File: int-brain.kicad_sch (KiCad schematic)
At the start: 34 parts, among them J1 PWR, J10 Conn_01x19_Pin, J11 Conn_01x19_Pin, J2 UART0, J3 I2C0, J4 PWR, J5 1MA, J6 1MB, J7 2MA, J8 2MB, J9 MPU9250, U2 ESP32-DevKitC, U4 LM2576HVT-5

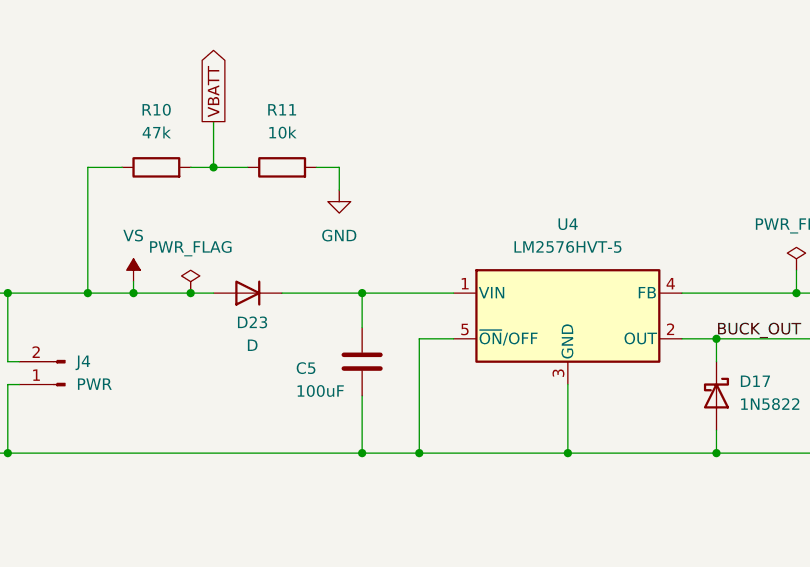
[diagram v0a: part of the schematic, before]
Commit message: placed PCB components
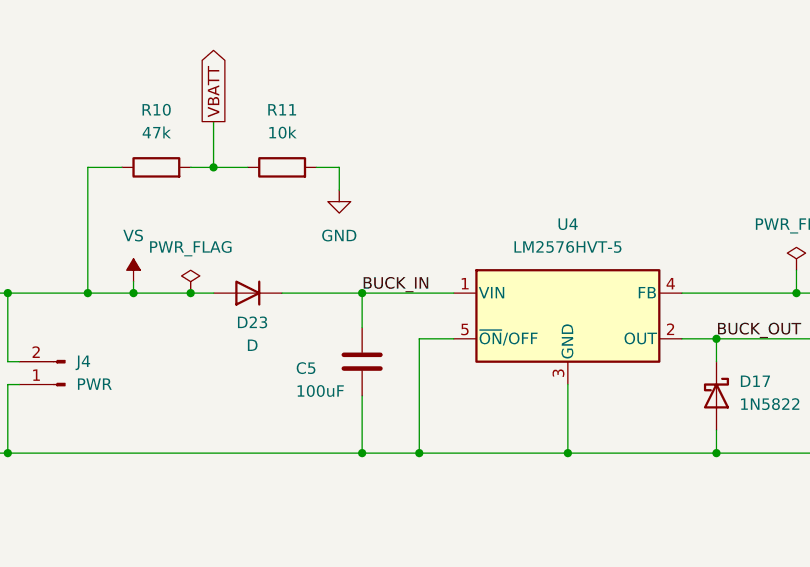
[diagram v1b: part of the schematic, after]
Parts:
- D18, D19, D20, D21, D22: footprint LED_THT:LED_D3.0mm -> LED_SMD:LED_0603_1608Metric_Pad1.05x0.95mm_HandSolder
- D23: footprint Diode_THT:D_DO-41_SOD81_P10.16mm_Horizontal -> Diode_SMD:D_SMA_Handsoldering
- R10, R11, R5, R6, R7, R8, R9: footprint Resistor_THT:R_Axial_DIN0207_L6.3mm_D2.5mm_P10.16mm_Horizontal -> Resistor_SMD:R_1206_3216Metric_Pad1.30x1.75mm_HandSolder
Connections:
- net BUCK_IN: now reaches C5.1, D23.1 (K), U4.1 (VIN)
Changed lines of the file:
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@@
 		)
 	)
+	(label "BUCK_IN"
+		(at 123.19 311.15 0)
+		(fields_autoplaced yes)
+		(effects
+			(font
+				(size 1.27 1.27)
+			)
+			(justify left bottom)
+		)
+	)
 	(label "1MB2"
 		(at 118.11 375.92 0)
@@
 			)
 		)
-		(property "Footprint" "LED_THT:LED_D3.0mm"
+		(property "Footprint" "LED_SMD:LED_0603_1608Metric_Pad1.05x0.95mm_HandSolder"
 			(at 257.81 146.05 0)
 			(effects
@@
 			)
 		)
-		(property "Footprint" "Resistor_THT:R_Axial_DIN0207_L6.3mm_D2.5mm_P10.16mm_Horizontal"
+		(property "Footprint" "Resistor_SMD:R_1206_3216Metric_Pad1.30x1.75mm_HandSolder"
 			(at 194.31 312.928 90)
 			(effects
@@
 			)
 		)
-		(property "Footprint" "Diode_THT:D_DO-41_SOD81_P10.16mm_Horizontal"
+		(property "Footprint" "Diode_SMD:D_SMA_Handsoldering"
 			(at 110.49 311.15 0)
 			(effects
@@
 			)
 		)
-		(property "Footprint" "Resistor_THT:R_Axial_DIN0207_L6.3mm_D2.5mm_P10.16mm_Horizontal"
+		(property "Footprint" "Resistor_SMD:R_1206_3216Metric_Pad1.30x1.75mm_HandSolder"
 			(at 238.252 134.62 90)
 			(effects
@@
 			)
 		)
-		(property "Footprint" "LED_THT:LED_D3.0mm"
+		(property "Footprint" "LED_SMD:LED_0603_1608Metric_Pad1.05x0.95mm_HandSolder"
 			(at 266.7 146.05 0)
 			(effects
@@
 			)
 		)
-		(property "Footprint" "LED_THT:LED_D3.0mm"
+		(property "Footprint" "LED_SMD:LED_0603_1608Metric_Pad1.05x0.95mm_HandSolder"
 			(at 248.92 146.05 0)
 			(effects
@@
 			)
 		)
-		(property "Footprint" "Resistor_THT:R_Axial_DIN0207_L6.3mm_D2.5mm_P10.16mm_Horizontal"
+		(property "Footprint" "Resistor_SMD:R_1206_3216Metric_Pad1.30x1.75mm_HandSolder"
 			(at 114.3 298.958 90)
 			(effects
@@
 			)
 		)
-		(property "Footprint" "Resistor_THT:R_Axial_DIN0207_L6.3mm_D2.5mm_P10.16mm_Horizontal"
+		(property "Footprint" "Resistor_SMD:R_1206_3216Metric_Pad1.30x1.75mm_HandSolder"
 			(at 256.032 134.62 90)
 			(effects
@@
 			)
 		)
-		(property "Footprint" "Resistor_THT:R_Axial_DIN0207_L6.3mm_D2.5mm_P10.16mm_Horizontal"
+		(property "Footprint" "Resistor_SMD:R_1206_3216Metric_Pad1.30x1.75mm_HandSolder"
 			(at 100.33 298.958 90)
 			(effects
@@
 			)
 		)
-		(property "Footprint" "Resistor_THT:R_Axial_DIN0207_L6.3mm_D2.5mm_P10.16mm_Horizontal"
+		(property "Footprint" "Resistor_SMD:R_1206_3216Metric_Pad1.30x1.75mm_HandSolder"
 			(at 264.922 134.62 90)
 			(effects
@@
 			)
 		)
-		(property "Footprint" "LED_THT:LED_D3.0mm"
+		(property "Footprint" "LED_SMD:LED_0603_1608Metric_Pad1.05x0.95mm_HandSolder"
 			(at 240.03 146.05 0)
 			(effects
@@
 			)
 		)
-		(property "Footprint" "LED_THT:LED_D3.0mm"
+		(property "Footprint" "LED_SMD:LED_0603_1608Metric_Pad1.05x0.95mm_HandSolder"
 			(at 200.66 321.31 0)
 			(effects
@@
 			)
 		)
-		(property "Footprint" "Resistor_THT:R_Axial_DIN0207_L6.3mm_D2.5mm_P10.16mm_Horizontal"
+		(property "Footprint" "Resistor_SMD:R_1206_3216Metric_Pad1.30x1.75mm_HandSolder"
 			(at 247.142 134.62 90)
 			(effects

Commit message: routing attempt
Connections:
- net BUCK_IN renamed VIN_BUCK
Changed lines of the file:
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@@
 		)
 	)
-	(label "BUCK_IN"
+	(label "VIN_BUCK"
 		(at 123.19 311.15 0)
 		(fields_autoplaced yes)

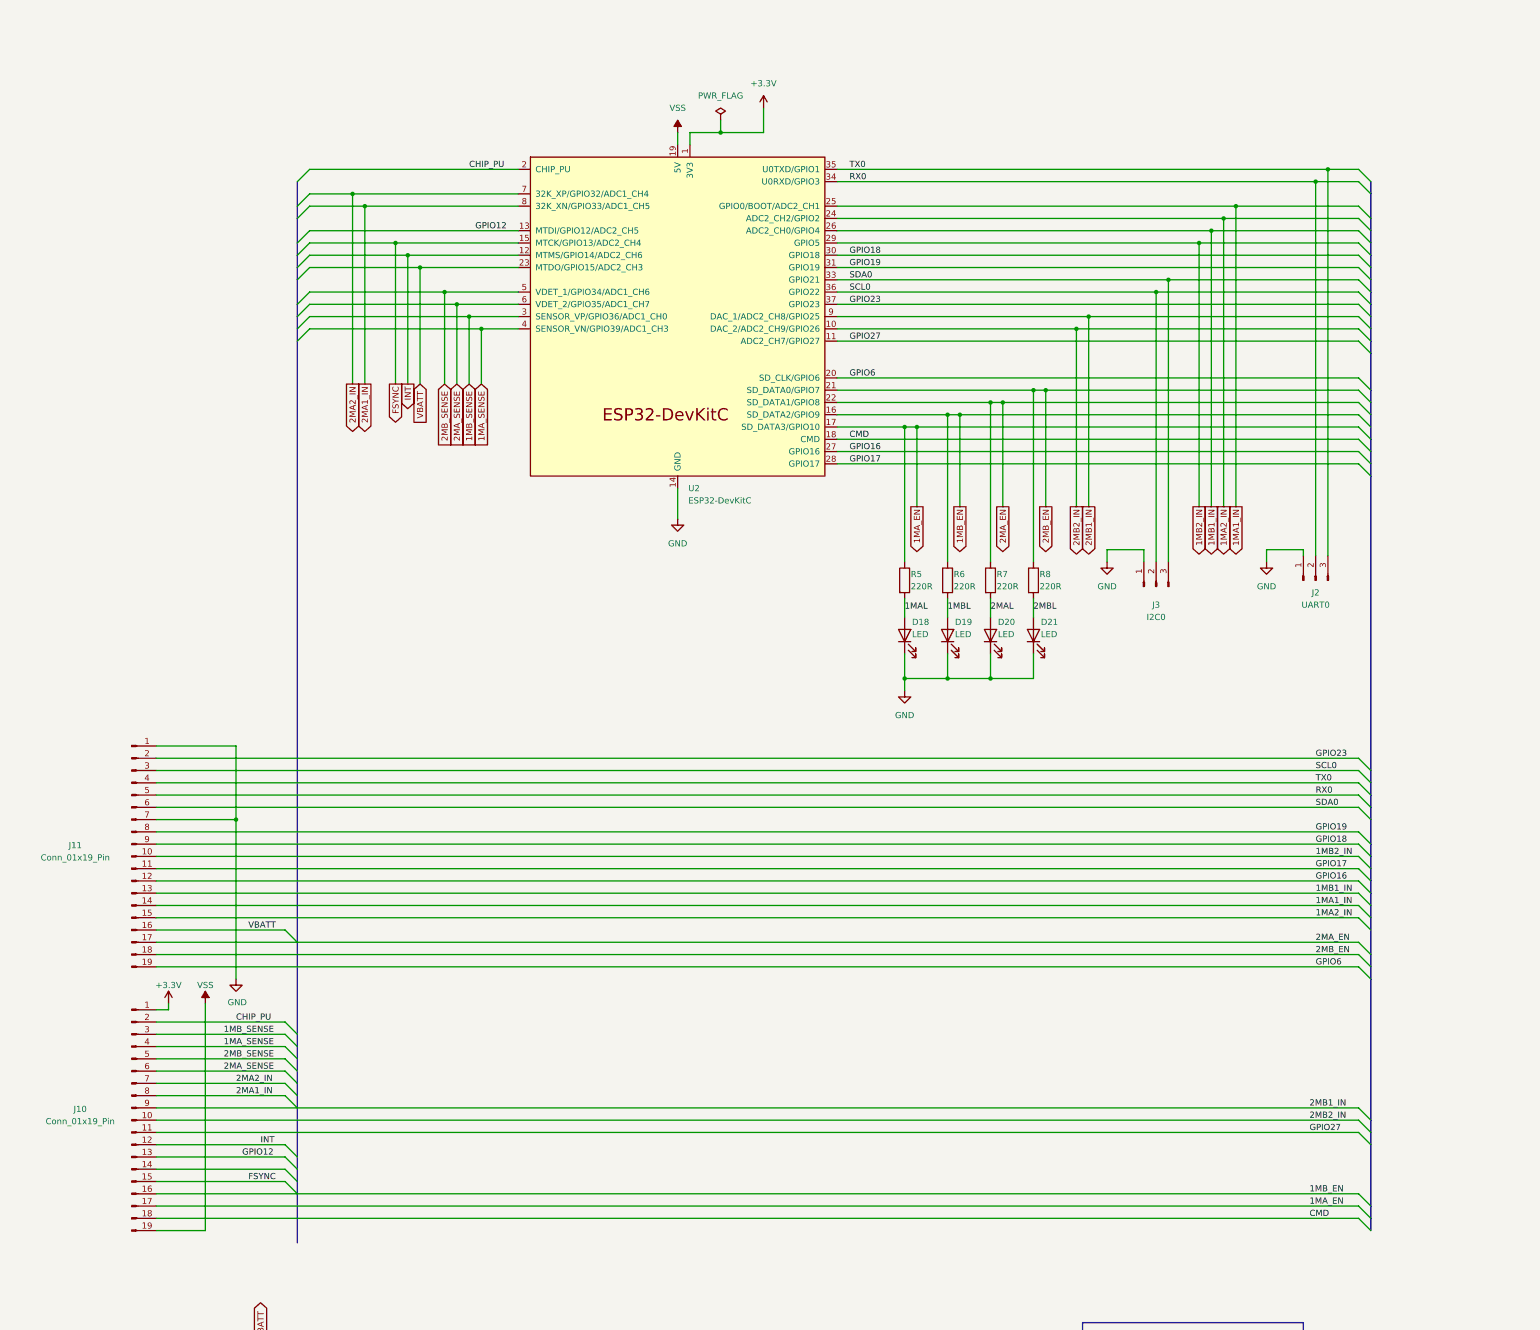
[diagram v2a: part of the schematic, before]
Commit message: re-do pinouts based on code
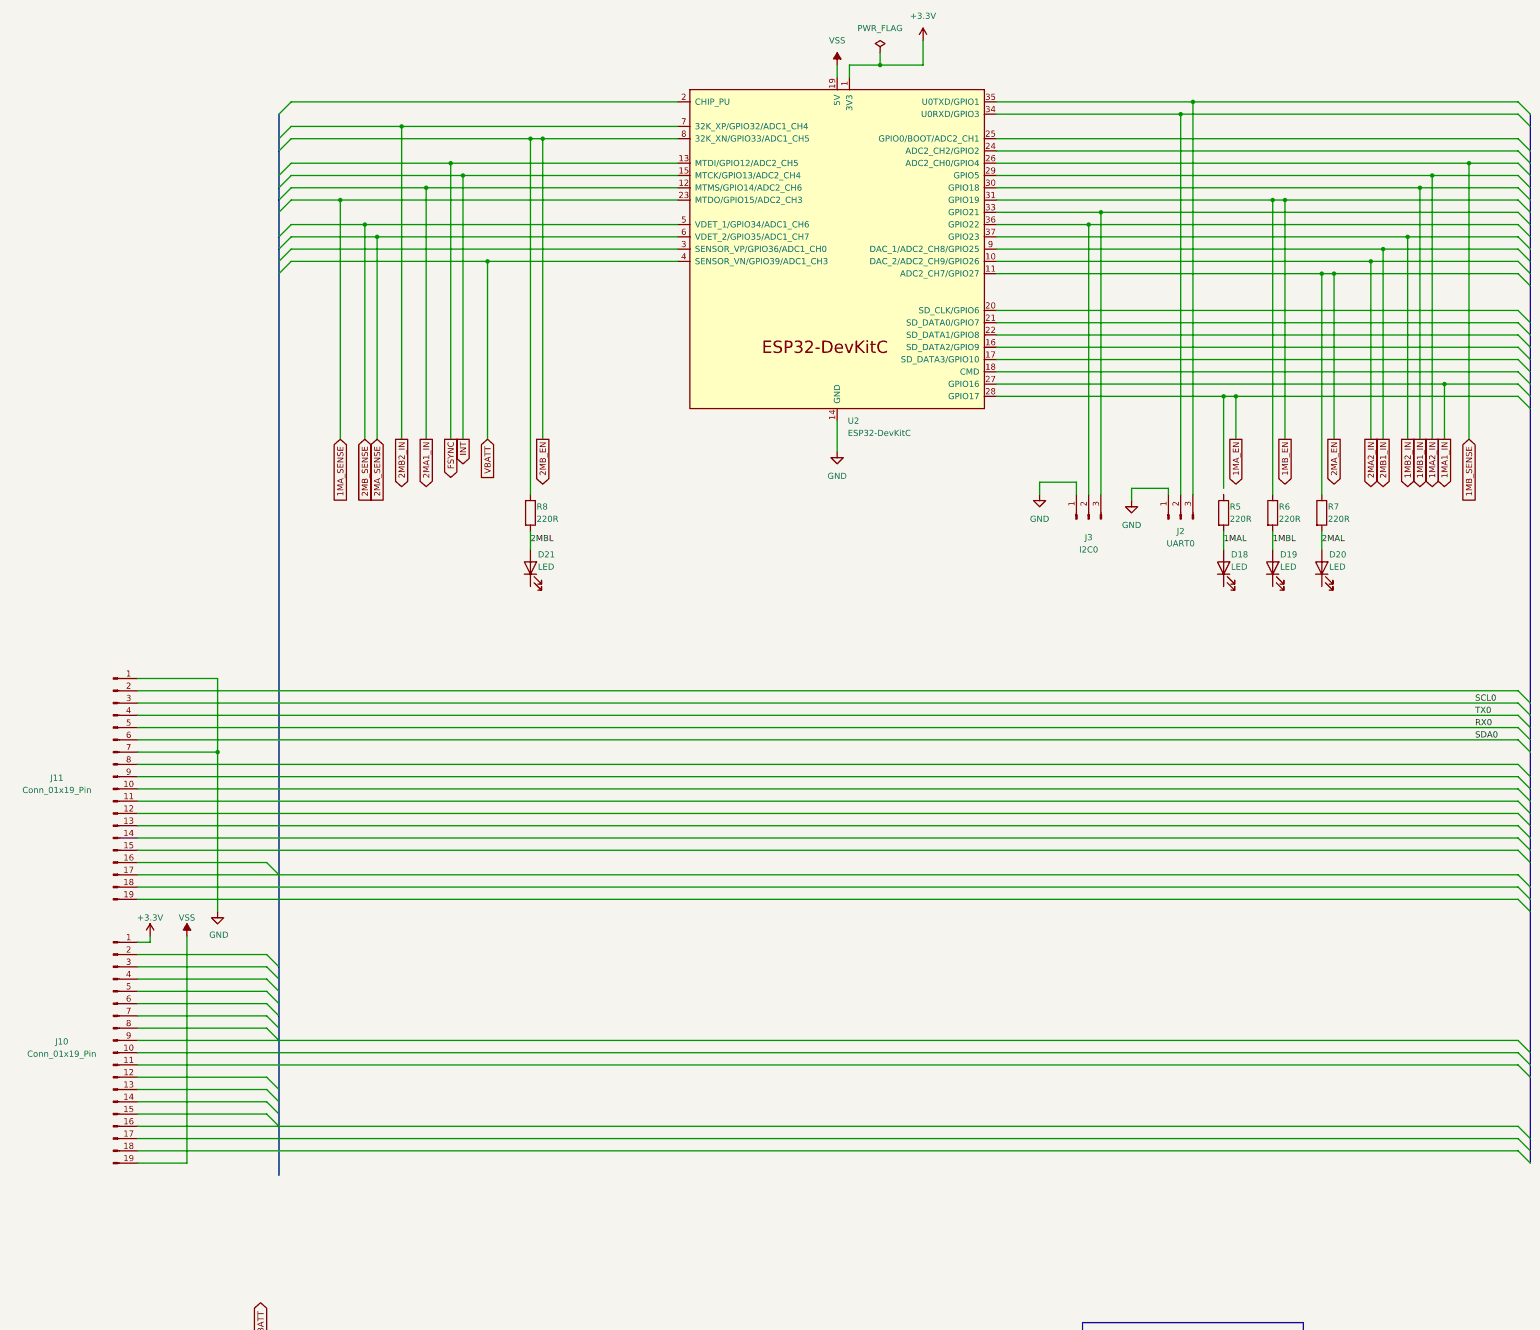
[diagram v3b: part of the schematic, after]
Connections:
- net 1MA1_IN: now also U2.27 (GPIO16); no longer J11.14 (Pin_14), U2.25 (GPIO0/BOOT/ADC2_CH1)
- net 1MA2_IN: now also U2.29 (GPIO5); no longer J11.15 (Pin_15), U2.24 (ADC2_CH2/GPIO2)
- net 1MA_EN: now also U2.28 (GPIO17); no longer J10.17 (Pin_17), R5.1, U2.17 (SD_DATA3/GPIO10)
- net 1MA_SENSE: now also U2.23 (MTDO/GPIO15/ADC2_CH3); no longer J10.4 (Pin_4), U2.4 (SENSOR_VN/GPIO39/ADC1_CH3)
- net 1MB1_IN: now also U2.30 (GPIO18); no longer J11.13 (Pin_13), U2.26 (ADC2_CH0/GPIO4)
- net 1MB2_IN: now also U2.37 (GPIO23); no longer J11.10 (Pin_10), U2.29 (GPIO5)
- net 1MB_EN: now also U2.31 (GPIO19); no longer J10.16 (Pin_16), U2.16 (SD_DATA2/GPIO9)
- net 1MB_SENSE: now also U2.26 (ADC2_CH0/GPIO4); no longer J10.3 (Pin_3), U2.3 (SENSOR_VP/GPIO36/ADC1_CH0)
- net 2MA1_IN: now also U2.12 (MTMS/GPIO14/ADC2_CH6); no longer J10.8 (Pin_8), U2.8 (32K_XN/GPIO33/ADC1_CH5)
- net 2MA2_IN: now also U2.10 (DAC_2/ADC2_CH9/GPIO26); no longer J10.7 (Pin_7), U2.7 (32K_XP/GPIO32/ADC1_CH4)
- net 2MA_EN: now also U2.11 (ADC2_CH7/GPIO27); no longer J11.17 (Pin_17), U2.22 (SD_DATA1/GPIO8)
- net 2MA_SENSE: no longer J10.6 (Pin_6)
- net 2MB1_IN: no longer J10.9 (Pin_9)
- net 2MB2_IN: now also U2.7 (32K_XP/GPIO32/ADC1_CH4); no longer J10.10 (Pin_10), U2.10 (DAC_2/ADC2_CH9/GPIO26)
- net 2MB_EN: now also U2.8 (32K_XN/GPIO33/ADC1_CH5); no longer J11.18 (Pin_18), U2.21 (SD_DATA0/GPIO7)
- net 2MB_SENSE: no longer J10.5 (Pin_5)
- net FSYNC: now also U2.13 (MTDI/GPIO12/ADC2_CH5); no longer J10.15 (Pin_15), U2.15 (MTCK/GPIO13/ADC2_CH4)
- net GND: no longer D18.1 (K), D19.1 (K), D20.1 (K), D21.1 (K)
- net INT: now also U2.15 (MTCK/GPIO13/ADC2_CH4); no longer J10.12 (Pin_12), U2.12 (MTMS/GPIO14/ADC2_CH6)
- net RX0: no longer J2.2 (Pin_2), U2.34 (U0RXD/GPIO3)
- net SCL0: no longer J3.2 (Pin_2), U2.36 (GPIO22)
- net SDA0: no longer J3.3 (Pin_3), U2.33 (GPIO21)
- net TX0: no longer J2.3 (Pin_3), U2.35 (U0TXD/GPIO1)
- net VBATT: now also U2.4 (SENSOR_VN/GPIO39/ADC1_CH3); no longer J11.16 (Pin_16), U2.23 (MTDO/GPIO15/ADC2_CH3)
- net CHIP_PU: no longer names the net of J10.2 (Pin_2)
- net CHIP_PU: no longer U2.2 (CHIP_PU)
- net CMD: no longer names the net of J10.18 (Pin_18)
- net CMD: no longer U2.18 (CMD)
- net GPIO12: no longer names the net of J10.13 (Pin_13)
- net GPIO12: no longer U2.13 (MTDI/GPIO12/ADC2_CH5)
- net GPIO16: no longer names the net of J11.12 (Pin_12)
- net GPIO16: no longer U2.27 (GPIO16)
- net GPIO17: no longer names the net of J11.11 (Pin_11)
- net GPIO17: no longer U2.28 (GPIO17)
- net GPIO18: no longer names the net of J11.9 (Pin_9)
- net GPIO18: no longer U2.30 (GPIO18)
- net GPIO19: no longer names the net of J11.8 (Pin_8)
- net GPIO19: no longer U2.31 (GPIO19)
- net GPIO23: no longer names the net of J11.2 (Pin_2)
- net GPIO23: no longer U2.37 (GPIO23)
- net GPIO27: no longer names the net of J10.11 (Pin_11)
- net GPIO27: no longer U2.11 (ADC2_CH7/GPIO27)
- net GPIO6: no longer names the net of J11.19 (Pin_19)
- net GPIO6: no longer U2.20 (SD_CLK/GPIO6)
- new net: J3.2 (Pin_2), U2.36 (GPIO22)
- new net: J3.3 (Pin_3), U2.33 (GPIO21)
- new net: J2.2 (Pin_2), U2.34 (U0RXD/GPIO3)
- new net: J2.3 (Pin_3), U2.35 (U0TXD/GPIO1)
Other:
- moved on the sheet: D18, D19, D20, D21, J10, J11, J2, J3, R5, R6, R7, R8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

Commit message: finish schematic rearrangement
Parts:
- J10: value Conn_01x19_Pin -> Left
- J11: value Conn_01x19_Pin -> Right
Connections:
- net 1MA1_IN: now also J11.12 (Pin_12)
- net 1MA2_IN: now also J11.10 (Pin_10)
- net 1MA_EN: now also J11.11 (Pin_11), R5.1
- net 1MA_SENSE: now also J11.16 (Pin_16)
- net 1MB1_IN: now also J11.9 (Pin_9)
- net 1MB2_IN: now also J11.2 (Pin_2)
- net 1MB_EN: now also J11.8 (Pin_8)
- net 1MB_SENSE: now also J11.13 (Pin_13)
- net 2MA1_IN: now also J10.12 (Pin_12)
- net 2MA2_IN: now also J10.10 (Pin_10)
- net 2MA_EN: now also J10.11 (Pin_11)
- net 2MA_SENSE: now also J10.6 (Pin_6)
- net 2MB1_IN: now also J10.9 (Pin_9)
- net 2MB2_IN: now also J10.7 (Pin_7)
- net 2MB_EN: now also J10.8 (Pin_8)
- net 2MB_SENSE: now also J10.5 (Pin_5)
- net FSYNC: now also J10.13 (Pin_13)
- net GND: now also D18.1 (K), D19.1 (K), D20.1 (K), D21.1 (K), J10.14 (Pin_14)
- net INT: now also J10.15 (Pin_15)
- net RX0: now also J2.2 (Pin_2), U2.34 (U0RXD/GPIO3)
- net SCL0: now also J3.2 (Pin_2), U2.36 (GPIO22)
- net SDA0: now also J3.3 (Pin_3), U2.33 (GPIO21)
- net TX0: now also J2.3 (Pin_3), U2.35 (U0TXD/GPIO1)
- net VBATT: now also J10.4 (Pin_4)
- net GPIO9: now reaches J10.16 (Pin_16)
- net GPIO9: now also U2.16 (SD_DATA2/GPIO9)
- net GPIO10: now reaches J10.17 (Pin_17)
- net GPIO10: now also U2.17 (SD_DATA3/GPIO10)
- net GPIO11: now reaches J10.18 (Pin_18)
- net GPIO11: now also U2.18 (CMD)
- net EN: now reaches J10.2 (Pin_2)
- net EN: now also U2.2 (CHIP_PU)
- net GPIO36: now reaches J10.3 (Pin_3)
- net GPIO36: now also U2.3 (SENSOR_VP/GPIO36/ADC1_CH0)
- net GPIO0: now reaches J11.14 (Pin_14)
- net GPIO0: now also U2.25 (GPIO0/BOOT/ADC2_CH1)
- net GPIO2: now reaches J11.15 (Pin_15)
- net GPIO2: now also U2.24 (ADC2_CH2/GPIO2)
- net GPIO8: now reaches J11.17 (Pin_17)
- net GPIO8: now also U2.22 (SD_DATA1/GPIO8)
- net GPIO7: now reaches J11.18 (Pin_18)
- net GPIO7: now also U2.21 (SD_DATA0/GPIO7)
- net GPIO6: now reaches J11.19 (Pin_19)
- net GPIO6: now also U2.20 (SD_CLK/GPIO6)

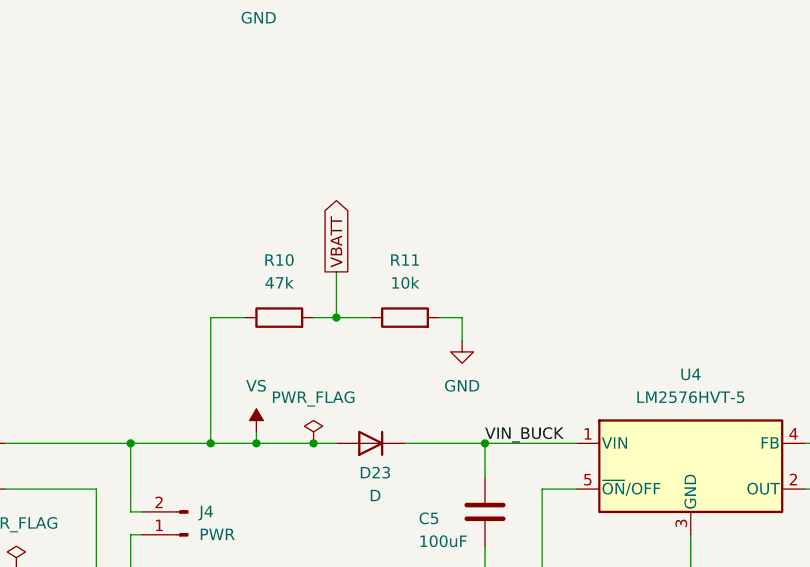
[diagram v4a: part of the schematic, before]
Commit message: set current sense resistors
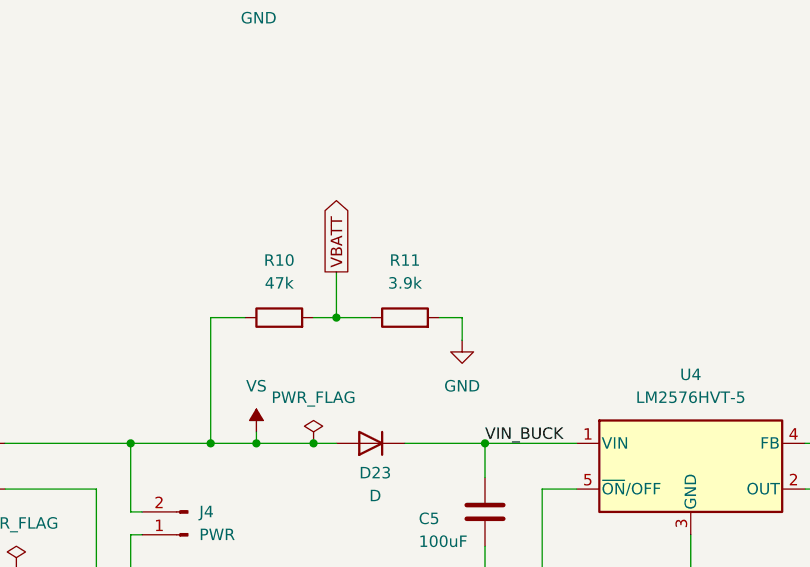
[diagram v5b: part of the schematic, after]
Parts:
- R11: value 10k -> 3.9k
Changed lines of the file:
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@@
 			)
 		)
-		(property "Value" "10k"
+		(property "Value" "3.9k"
 			(at 114.3 293.37 90)
 			(effects
